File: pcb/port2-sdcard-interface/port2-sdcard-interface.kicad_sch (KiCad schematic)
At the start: 55 parts, among them J2 P2000T Port 2, J3 SD Card, U1 CY62128ELL-45SXI, U10 74HC32, U11 74HC273, U12 74HC165, U13 74HC595, U14 74HC00, U15 SST39SF010, U17 74HC138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

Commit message: Setting port addresses in header and include files
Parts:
- removed J3: SD Card, Connector_PinSocket_2.54mm:PinSocket_1x06_P2.54mm_Vertical, symbol Connector:Conn_01x06_Socket
- added C23: 100nF, Capacitor_SMD:C_1206_3216Metric_Pad1.33x1.80mm_HandSolder, symbol Device:C
- added J1: Micro_SD_Card_Det1, components:CONN9_MSD-1_CUD, symbol Connector:Micro_SD_Card_Det1
- added R10, R11, R8, R9: 3.3k, Resistor_SMD:R_0805_2012Metric_Pad1.20x1.40mm_HandSolder, symbol Device:R
- added U16: AMS1117-3.3, Package_TO_SOT_SMD:SOT-223-3_TabPin2, symbol Regulator_Linear:AMS1117-3.3
- added U21: 74LVC125, Package_SO:TSSOP-14_4.4x5mm_P0.65mm, symbol 74xx:74LVC125
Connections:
- net CLK: now also R10.1
- net GND: now also U20.12 (A1), C23.2, J1.6 (VSS), U16.1 (GND), U21.1, U21.10, U21.13, U21.4, U21.7 (GND)
- net MISO: now also U21.11
- net MOSI: now also R9.1
- net VCC: now also U16.3 (VI); no longer U20.12 (A1)
- net ~{CS}: now also R11.1
- new net: R11.2, U21.9
- new net: R10.2, U21.5
- new net: R8.2, U21.12
- new net: R9.2, U21.2
- new net +3V3: C23.1, J1.4 (VDD), U16.2 (VO), U21.14 (VCC)
- new net CS_LLS: J1.2 (DAT3/CD), U21.8
- new net D0_LLS: J1.7 (DAT0), R8.1
- new net DI_LLS: J1.3 (CMD), U21.3
- new net SCK_LLS: J1.5 (CLK), U21.6
- no-connect marks 24 -> 28
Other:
- note added: "Note: 74LVC125 needs 3v3 on VCC"
- moved on the sheet: J2, U19E, U20, U7C

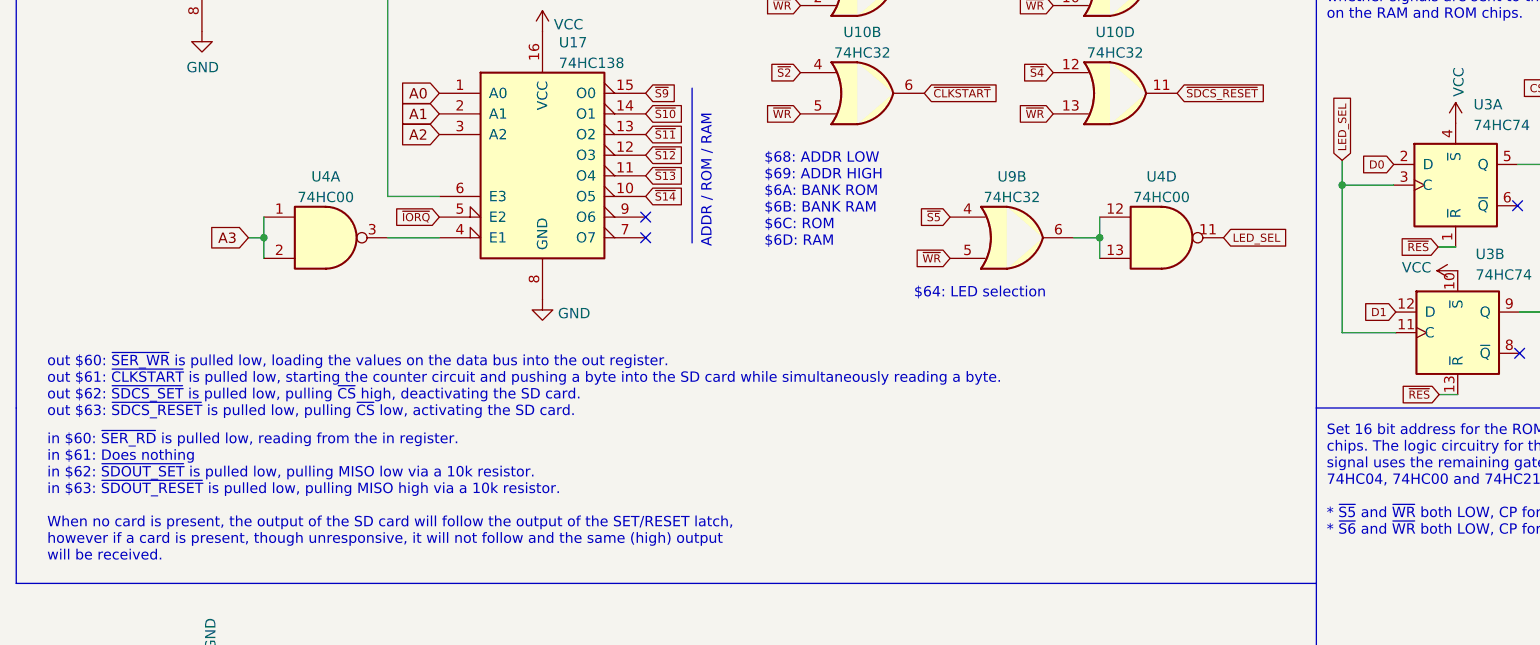
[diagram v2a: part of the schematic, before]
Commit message: Updating rev and changing 0x60 to 0x40
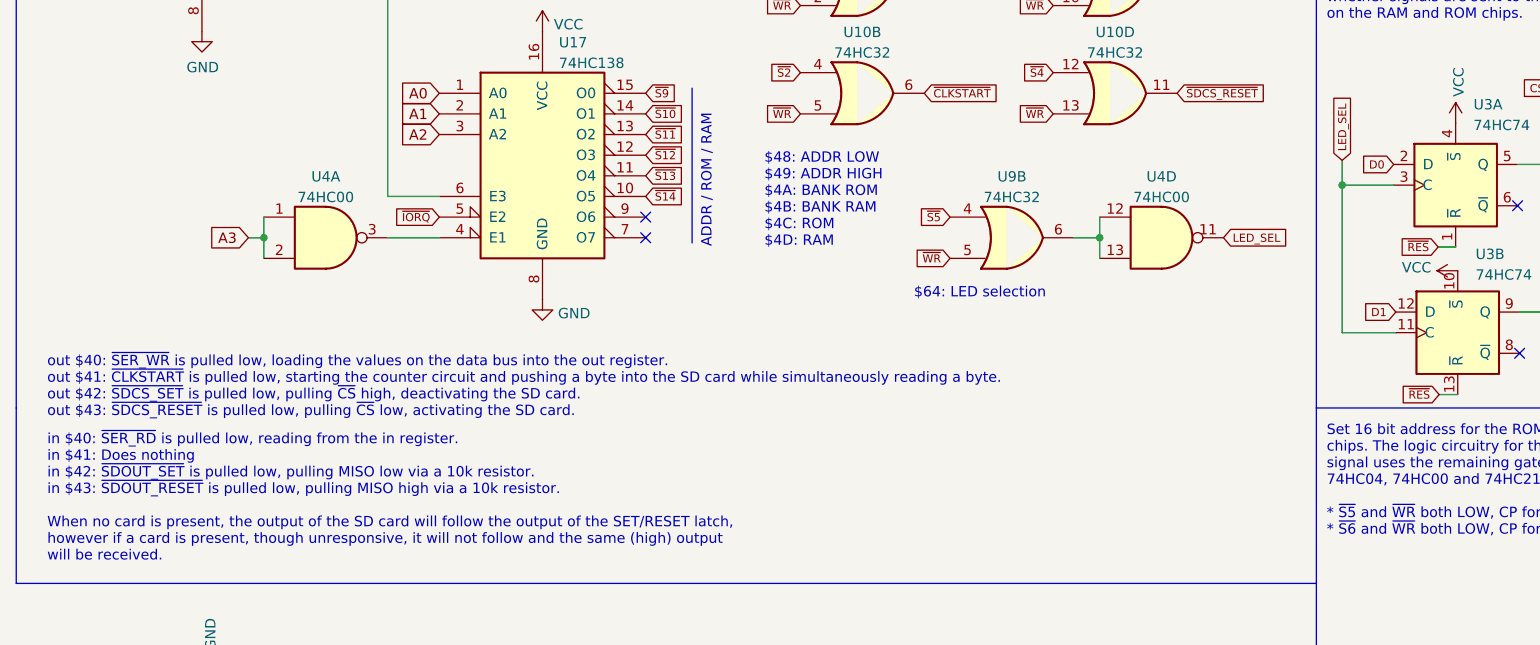
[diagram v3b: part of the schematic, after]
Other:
- note added: "$48: ADDR LOW $49: ADDR HIGH $4A: BANK ROM $4B: BANK RAM $4C: ROM $4D: RAM"
- note added: "in $40: ~{SER_RD} is pulled low, reading from the in register. in $41: Does nothing in $42: ~{SDOUT_SET} is pulled low, pulling MISO low via a 10k resistor. in $43: ~{SDOUT_RESET} is pulled low, pulling MISO high via a 10k resistor. When no card is present, the output of the SD card will follow the output of the SET/RESET latch, however if a card is present, though unresponsive, it will not follo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"
- note added: "out $40: ~{SER_WR} is pulled low, loading the values on the data bus into the out register. out $41: ~{CLKSTART} is pulled low, starting the counter circuit and pushing a byte into the SD card while simultaneously reading a byte. out $42: ~{SDCS_SET} is pulled low, pulling ~{CS} high, deactivating the SD card. out $43: ~{SDCS_RESET} is pulled low, pulling ~{CS} low, activating the SD card."
- note removed: "$68: ADDR LOW $69: ADDR HIGH $6A: BANK ROM $6B: BANK RAM $6C: ROM $6D: RAM"
- note removed: "in $60: ~{SER_RD} is pulled low, reading from the in register. in $61: Does nothing in $62: ~{SDOUT_SET} is pulled low, pulling MISO low via a 10k resistor. in $63: ~{SDOUT_RESET} is pulled low, pulling MISO high via a 10k resistor. When no card is present, the output of the SD card will follow the output of the SET/RESET latch, however if a card is present, though unresponsive, it will not follo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"
- note removed: "out $60: ~{SER_WR} is pulled low, loading the values on the data bus into the out register. out $61: ~{CLKSTART} is pulled low, starting the counter circuit and pushing a byte into the SD card while simultaneously reading a byte. out $62: ~{SDCS_SET} is pulled low, pulling ~{CS} high, deactivating the SD card. out $63: ~{SDCS_RESET} is pulled low, pulling ~{CS} low, activating the SD card."
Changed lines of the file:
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@@
 	(title_block
 		(title "Philips P2000T SD-CARD SLOT2 cartridge")
-		(date "2024-05-10")
-		(rev "rev5")
+		(date "2024-05-26")
+		(rev "rev6")
 	)
 		(symbol "Device:C"
@@
 		)
 	)
-	(text "out $60: ~{SER_WR} is pulled low, loading the values on the data bus into the out register.\nout $61: ~{CLKSTART} is pulled low, starting the counter circuit and pushing a byte into the SD card while simultaneously reading a byte.\nout $62: ~{SDCS_SET} is pulled low, pulling ~{CS} high, deactivating the SD card.\nout $63: ~{SDCS_RESET} is pulled low, pulling ~{CS} low, activating the SD card."
+	(text "out $40: ~{SER_WR} is pulled low, loading the values on the data bus into the out register.\nout $41: ~{CLKSTART} is pulled low, starting the counter circuit and pushing a byte into the SD card while simultaneously reading a byte.\nout $42: ~{SDCS_SET} is pulled low, pulling ~{CS} high, deactivating the SD card.\nout $43: ~{SDCS_RESET} is pulled low, pulling ~{CS} low, activating the SD card."
 		(exclude_from_sim no)
 		(at 19.05 172.085 0)
@@
 		)
 	)
-	(text "in $60: ~{SER_RD} is pulled low, reading from the in register.\nin $61: Does nothing\nin $62: ~{SDOUT_SET} is pulled low, pulling MISO low via a 10k resistor.\nin $63: ~{SDOUT_RESET} is pulled low, pulling MISO high via a 10k resistor.\n\nWhen no card is present, the output of the SD card will follow the output of the SET/RESET latch,\nhowever if a card is present, though unresponsive, it will not follow and the same (high) output\nwill be received."
+	(text "in $40: ~{SER_RD} is pulled low, reading from the in register.\nin $41: Does nothing\nin $42: ~{SDOUT_SET} is pulled low, pulling MISO low via a 10k resistor.\nin $43: ~{SDOUT_RESET} is pulled low, pulling MISO high via a 10k resistor.\n\nWhen no card is present, the output of the SD card will follow the output of the SET/RESET latch,\nhowever if a card is present, though unresponsive, it will not follow and the same (high) output\nwill be received."
 		(exclude_from_sim no)
 		(at 19.05 189.865 0)
@@
 		)
 	)
-	(text "$68: ADDR LOW\n$69: ADDR HIGH\n$6A: BANK ROM\n$6B: BANK RAM\n$6C: ROM\n$6D: RAM\n"
+	(text "$48: ADDR LOW\n$49: ADDR HIGH\n$4A: BANK ROM\n$4B: BANK RAM\n$4C: ROM\n$4D: RAM\n"
 		(exclude_from_sim no)
 		(at 107.315 151.13 0)
